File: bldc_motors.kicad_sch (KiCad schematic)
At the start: 0 parts

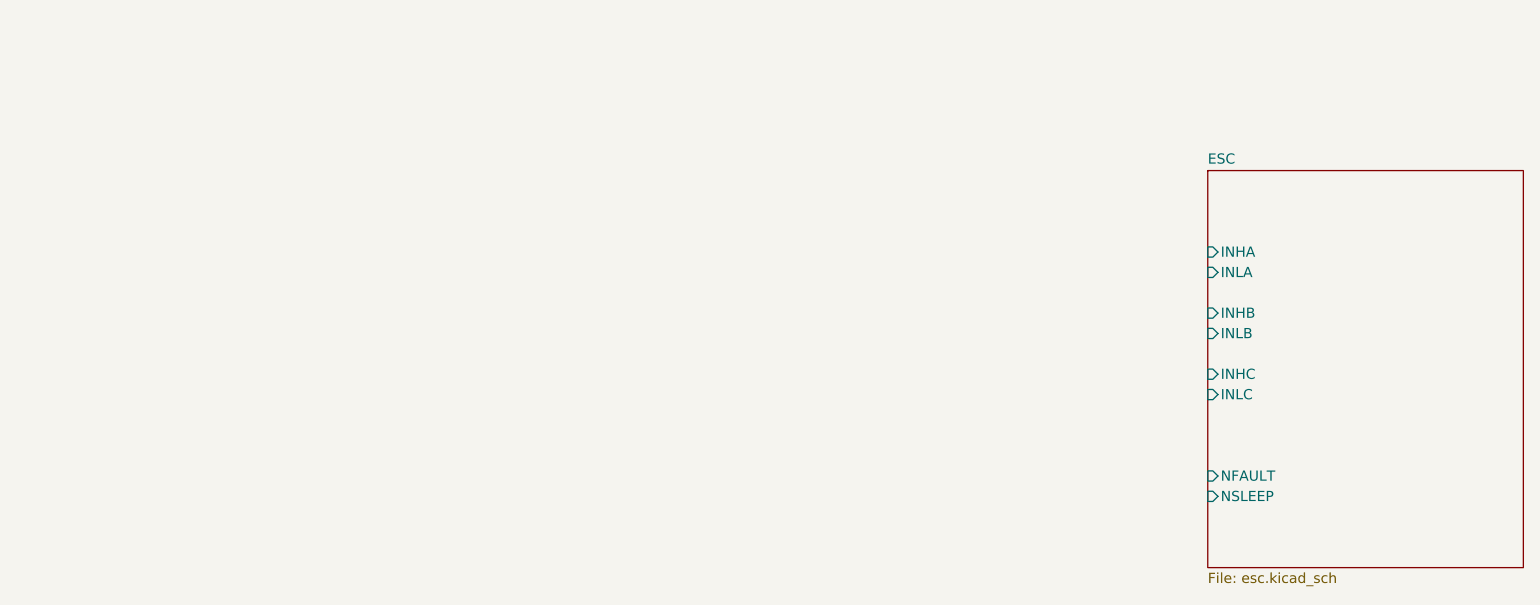
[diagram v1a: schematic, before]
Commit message: Reorder gate driver symbol and rearrange ESC
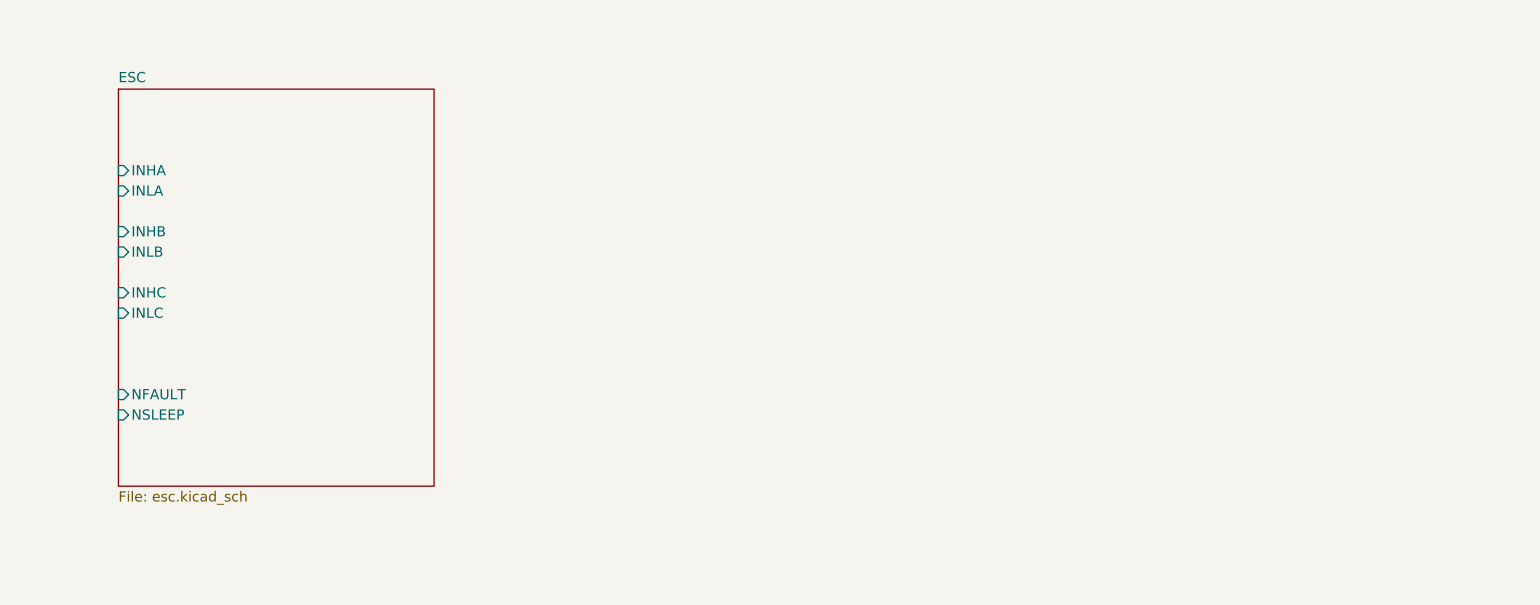
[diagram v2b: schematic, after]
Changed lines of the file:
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@@
 	(paper "A4")
 	(sheet
-		(at 168.91 36.83)
+		(at 33.02 26.67)
 		(size 39.37 49.53)
 		(exclude_from_sim no)
@@
 		)
 		(property "Sheetname" "ESC"
-			(at 168.91 36.1184 0)
+			(at 33.02 25.9584 0)
 			(show_name no)
 			(do_not_autoplace no)
@@
 		)
 		(property "Sheetfile" "esc.kicad_sch"
-			(at 168.91 86.9446 0)
+			(at 33.02 76.7846 0)
 			(show_name no)
 			(do_not_autoplace no)
@@
 		)
 		(pin "NFAULT" input
-			(at 168.91 74.93 180)
+			(at 33.02 64.77 180)
 			(effects
 				(font
@@
 		)
 		(pin "INLA" input
-			(at 168.91 49.53 180)
+			(at 33.02 39.37 180)
 			(effects
 				(font
@@
 		)
 		(pin "INHB" input
-			(at 168.91 54.61 180)
+			(at 33.02 44.45 180)
 			(effects
 				(font
@@
 		)
 		(pin "NSLEEP" input
-			(at 168.91 77.47 180)
+			(at 33.02 67.31 180)
 			(effects
 				(font
@@
 		)
 		(pin "INLC" input
-			(at 168.91 64.77 180)
+			(at 33.02 54.61 180)
 			(effects
 				(font
@@
 		)
 		(pin "INHC" input
-			(at 168.91 62.23 180)
+			(at 33.02 52.07 180)
 			(effects
 				(font
@@
 		)
 		(pin "INLB" input
-			(at 168.91 57.15 180)
+			(at 33.02 46.99 180)
 			(effects
 				(font
@@
 		)
 		(pin "INHA" input
-			(at 168.91 46.99 180)
+			(at 33.02 36.83 180)
 			(effects
 				(font
@@
 		)
 	)
-	(embedded_fonts no)
 )

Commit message: Various little adjustments to ESC
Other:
- sheet ESC ports: added +BATT, 3V3, DSHOT, GND, TELEMETRY; removed INHA, INHB, INHC, INLA, INLB, INLC, NFAULT, NSLEEP
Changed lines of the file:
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@@
 	(paper "A4")
 	(sheet
-		(at 33.02 26.67)
-		(size 39.37 49.53)
+		(at 20.32 20.32)
+		(size 19.05 26.67)
 		(exclude_from_sim no)
 		(in_bom yes)
@@
 		)
 		(property "Sheetname" "ESC"
-			(at 33.02 25.9584 0)
+			(at 20.32 19.6084 0)
 			(show_name no)
 			(do_not_autoplace no)
@@
 		)
 		(property "Sheetfile" "esc.kicad_sch"
-			(at 33.02 76.7846 0)
+			(at 20.32 47.5746 0)
 			(show_name no)
 			(do_not_autoplace no)
@@
 			)
 		)
-		(pin "NFAULT" input
-			(at 33.02 64.77 180)
+		(pin "DSHOT" input
+			(at 20.32 31.75 180)
 			(effects
 				(font
@@
 			)
 		)
-		(pin "INLA" input
-			(at 33.02 39.37 180)
+		(pin "TELEMETRY" input
+			(at 20.32 35.56 180)
 			(effects
 				(font
@@
 			)
 		)
-		(pin "INHB" input
-			(at 33.02 44.45 180)
+		(pin "+BATT" input
+			(at 33.02 20.32 90)
 			(effects
 				(font
 					(size 1.27 1.27)
 				)
-				(justify left)
+				(justify right)
 			)
 		)
-		(pin "NSLEEP" input
-			(at 33.02 67.31 180)
+		(pin "3V3" input
+			(at 26.67 20.32 90)
 			(effects
 				(font
 					(size 1.27 1.27)
 				)
-				(justify left)
+				(justify right)
 			)
 		)
-		(pin "INLC" input
-			(at 33.02 54.61 180)
+		(pin "GND" input
+			(at 29.21 46.99 270)
 			(effects
 				(font
-					(size 1.27 1.27)
-				)
-				(justify left)
-			)
-		)
-		(pin "INHC" input
-			(at 33.02 52.07 180)
-			(effects
-				(font
-					(size 1.27 1.27)
-				)
-				(justify left)
-			)
-		)
-		(pin "INLB" input
-			(at 33.02 46.99 180)
-			(effects
-				(font
-					(size 1.27 1.27)
-				)
-				(justify left)
-			)
-		)
-		(pin "INHA" input
-			(at 33.02 36.83 180)
-			(effects
-				(font
